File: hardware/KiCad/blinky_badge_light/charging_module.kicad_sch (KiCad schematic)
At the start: 17 parts, among them Q1 N-Channel MOSFET, Q3 N-Channel MOSFET, Q4 Q_PMOS_GSD, U2 TP4056

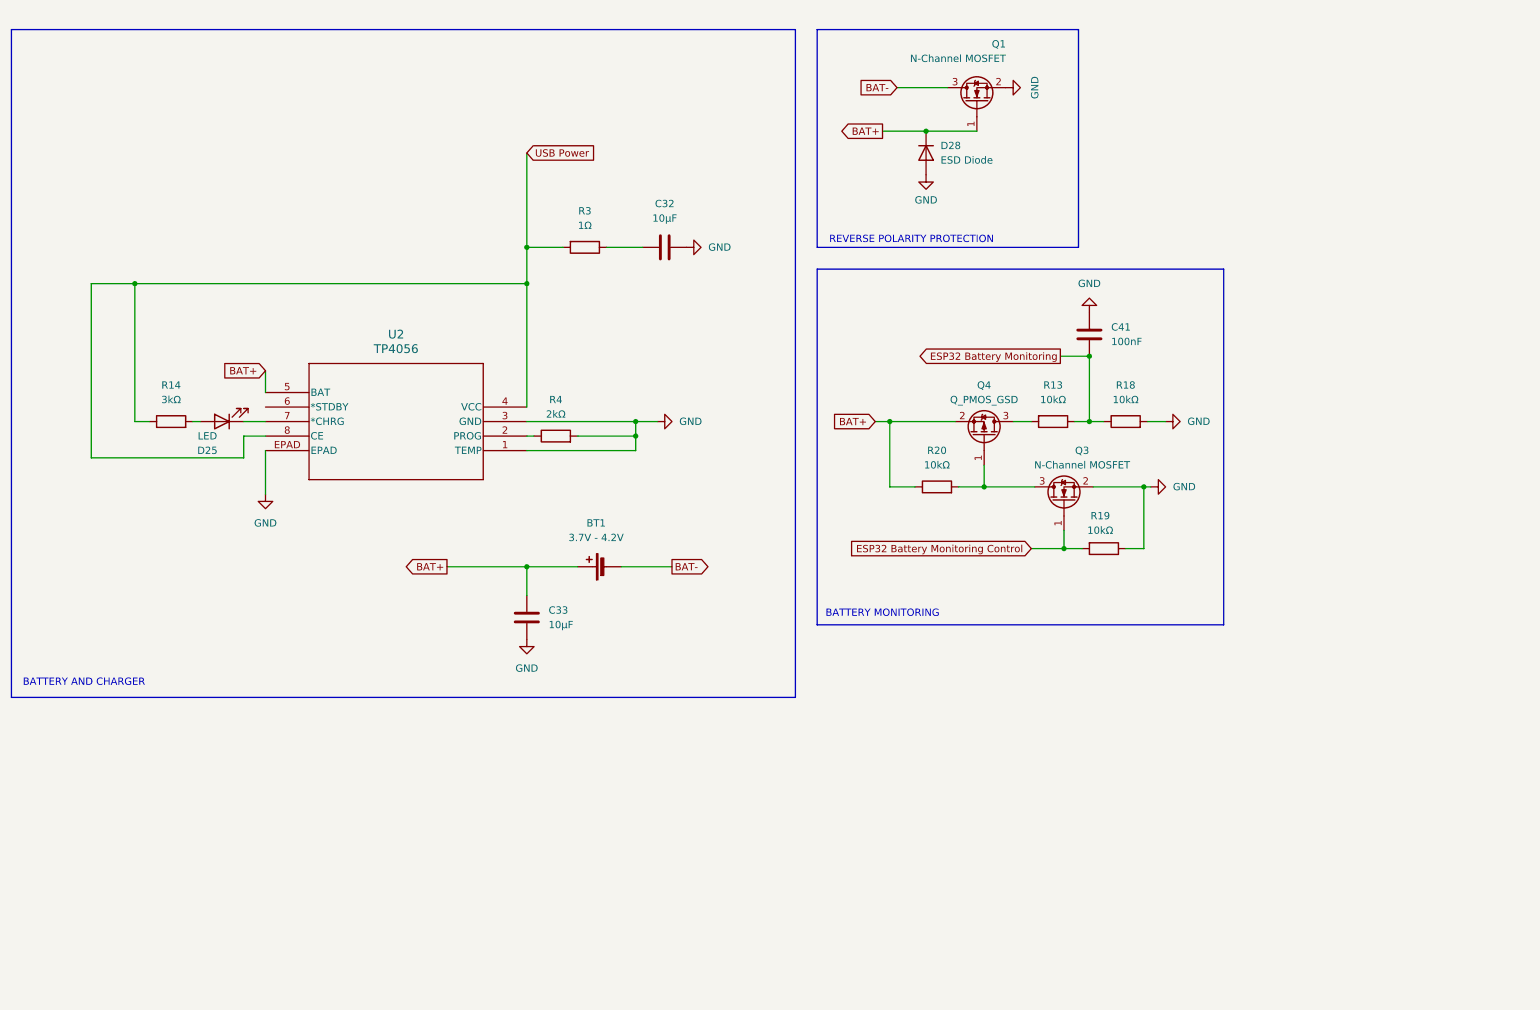
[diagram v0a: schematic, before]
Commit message: much more complicated button logic now
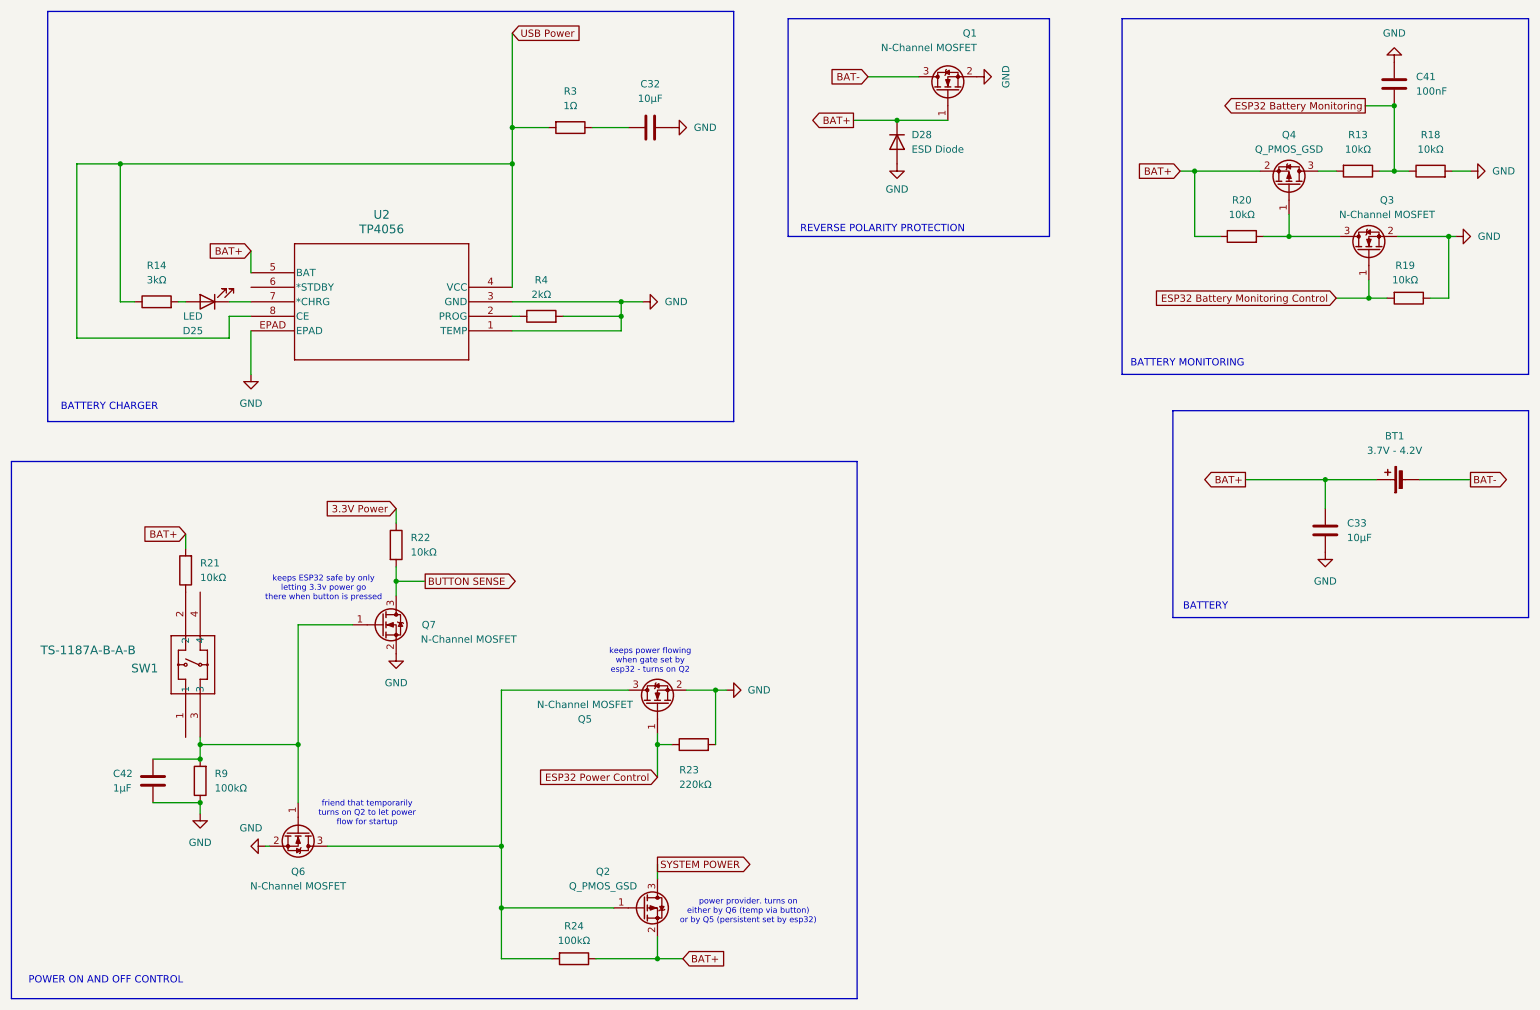
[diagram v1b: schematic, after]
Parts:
- added C42: 1µF, Capacitor_SMD:C_0603_1608Metric, symbol Device:C
- added Q2: Q_PMOS_GSD, Package_TO_SOT_SMD:SOT-23, symbol Device:Q_PMOS_GSD
- added Q5, Q6, Q7: N-Channel MOSFET, footprints:SOT-23-3_L2.9-W1.3-P1.90-LS2.4-BR, symbol Transistor_FET:AO3400A
- added R21, R22: 10kΩ, Resistor_SMD:R_0603_1608Metric, symbol Device:R
- added R23: 220kΩ, Resistor_SMD:R_0603_1608Metric, symbol Device:R
- added R24, R9: 100kΩ, Resistor_SMD:R_0603_1608Metric, symbol Device:R
- added SW1: TS-1187A-B-A-B, footprints:SW-SMD_4P-L5.1-W5.1-P3.70-LS6.5-TL_H1.5, symbol 2025-02-08_13-23-39:TS-1187A-B-A-B
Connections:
- net BAT+: now also Q2.2 (S), R21.2, R24.1
- net GND: now also C42.1, Q5.2 (S), Q6.2 (S), Q7.2 (S), R23.2, R9.1
- new net: C42.2, Q6.1 (G), Q7.1 (G), R9.2, SW1.3
- new net: Q2.1 (G), Q5.3 (D), Q6.3 (D), R24.2
- new net: R21.1, SW1.2
- new net 3.3V Power: R22.1
- new net BUTTON SENSE: Q7.3 (D), R22.2
- new net ESP32 Power Control: Q5.1 (G), R23.1
- new net SYSTEM POWER: Q2.3 (D)
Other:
- note added: "BATTERY"
- note added: "BATTERY CHARGER"
- note added: "POWER ON AND OFF CONTROL"
- note added: "friend that temporarily turns on Q2 to let power flow for startup"
- note added: "keeps ESP32 safe by only letting 3.3v power go there when button is pressed"
- note added: "keeps power flowing when gate set by esp32 - turns on Q2"
- note added: "power provider. turns on either by Q6 (temp via button) or by Q5 (persistent set by esp32)"
- note removed: "BATTERY AND CHARGER"
- moved on the sheet: BT1, C32, C33, C41, D25, D28, Q1, Q3, Q4, R13, R14, R18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
